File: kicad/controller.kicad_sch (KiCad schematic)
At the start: 26 parts, among them U1 RP2040, U2 W25Q16JVUXIQ, Y1 Crystal_GND24

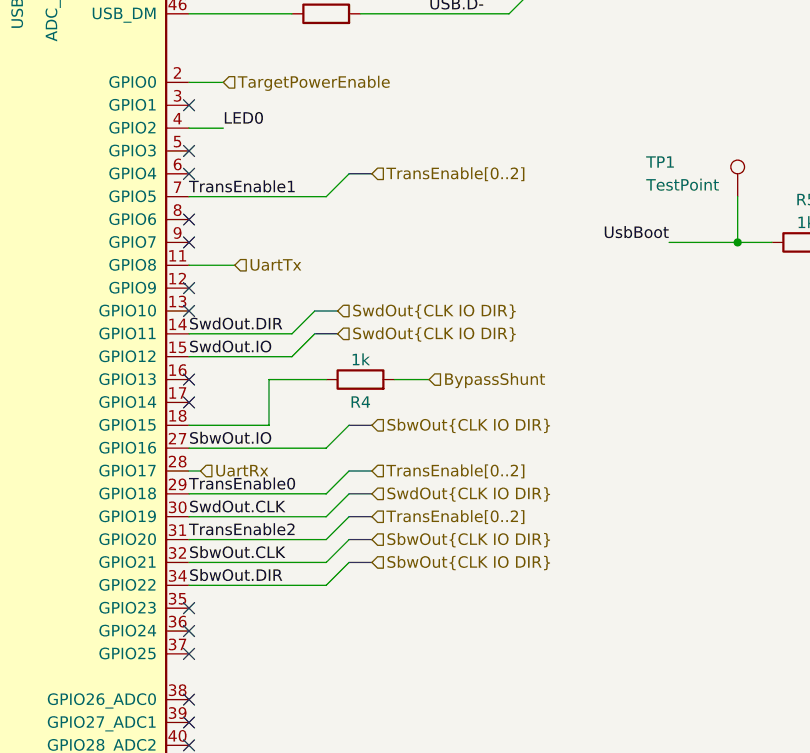
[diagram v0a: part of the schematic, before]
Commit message: add fourth level converter for simultaneous programming + TX/RX
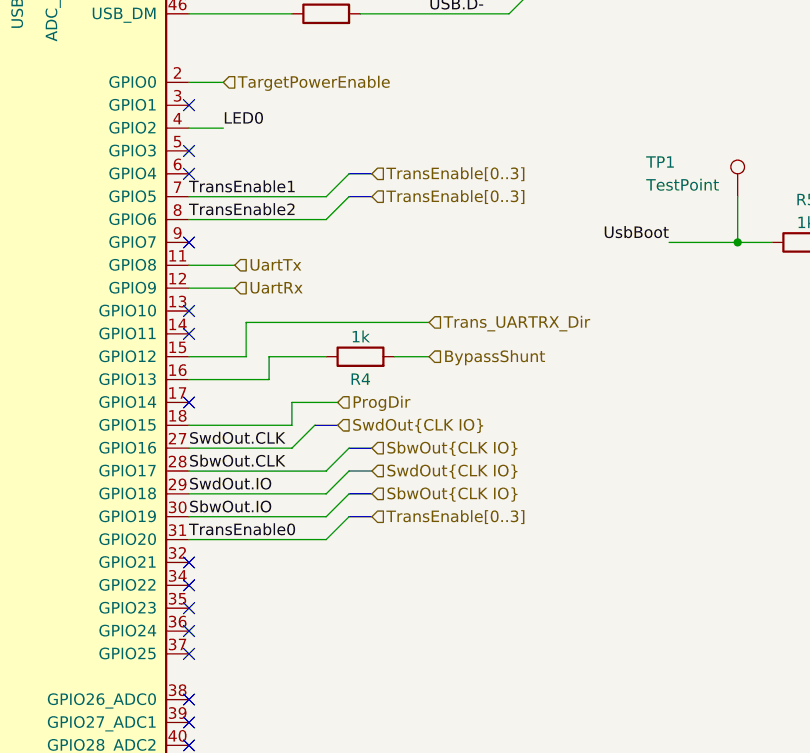
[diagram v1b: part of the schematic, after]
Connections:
- net SbwOut.CLK: now also U1.28 (GPIO17); no longer U1.32 (GPIO21)
- net SbwOut.IO: now also U1.30 (GPIO19); no longer U1.27 (GPIO16)
- net SwdOut.CLK: now also U1.27 (GPIO16); no longer U1.30 (GPIO19)
- net SwdOut.IO: now also U1.29 (GPIO18); no longer U1.15 (GPIO12)
- net TransEnable0: now also U1.31 (GPIO20); no longer U1.29 (GPIO18)
- net TransEnable2: now also U1.8 (GPIO6); no longer U1.31 (GPIO20)
- net UartRx: now also U1.12 (GPIO9); no longer U1.28 (GPIO17)
- net at R4.1: now also U1.16 (GPIO13); no longer U1.18 (GPIO15)
- net SbwOut.DIR: no longer names the net of U1.34 (GPIO22)
- net SwdOut.DIR: no longer names the net of U1.14 (GPIO11)
- new net ProgDir: U1.18 (GPIO15)
- new net Trans_UARTRX_Dir: U1.15 (GPIO12)
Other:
- moved on the sheet: R4

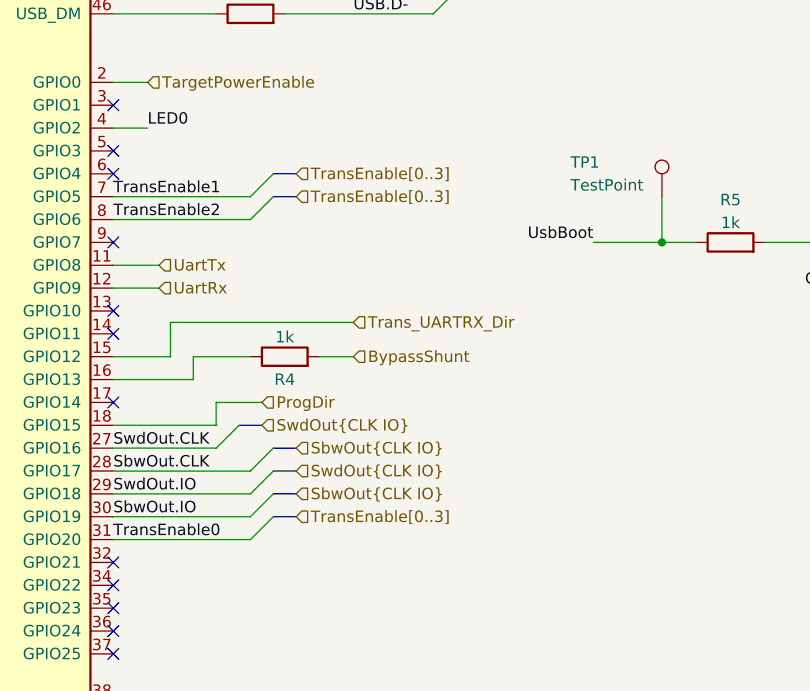
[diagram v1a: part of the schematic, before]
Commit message: fix some net names
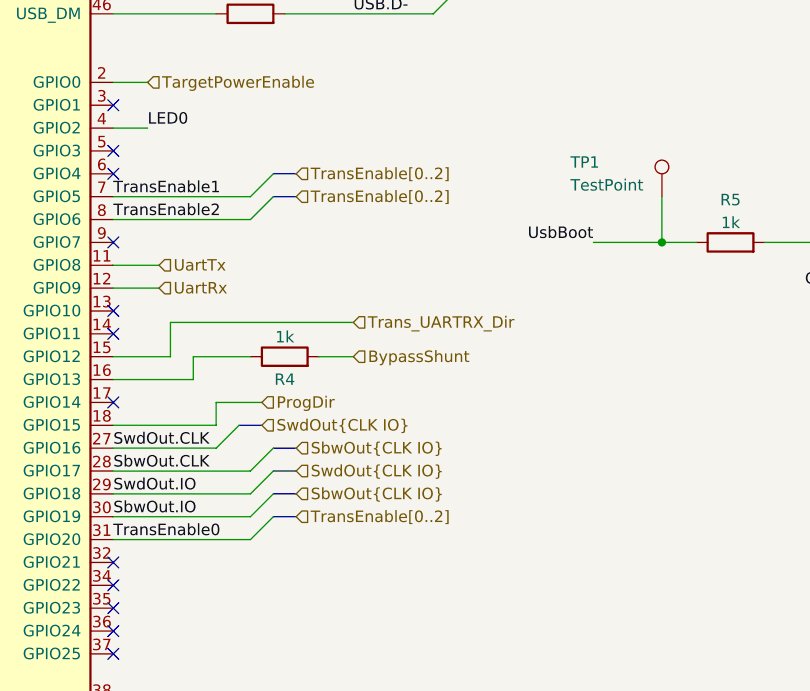
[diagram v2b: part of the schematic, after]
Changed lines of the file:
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@@
     (effects (font (size 1.27 1.27)) (justify left bottom))
   )
-  (hierarchical_label "TransEnable[0..3]" (shape input) (at 171.45 143.51 0)
+  (hierarchical_label "TransEnable[0..2]" (shape input) (at 171.45 143.51 0)
     (effects (font (size 1.27 1.27)) (justify left))
   )
@@
     (effects (font (size 1.27 1.27)) (justify left))
   )
-  (hierarchical_label "TransEnable[0..3]" (shape input) (at 171.45 105.41 0)
+  (hierarchical_label "TransEnable[0..2]" (shape input) (at 171.45 105.41 0)
     (effects (font (size 1.27 1.27)) (justify left))
   )
@@
     (effects (font (size 1.27 1.27)) (justify left))
   )
-  (hierarchical_label "TransEnable[0..3]" (shape input) (at 171.45 107.95 0)
+  (hierarchical_label "TransEnable[0..2]" (shape input) (at 171.45 107.95 0)
     (effects (font (size 1.27 1.27)) (justify left))
   )

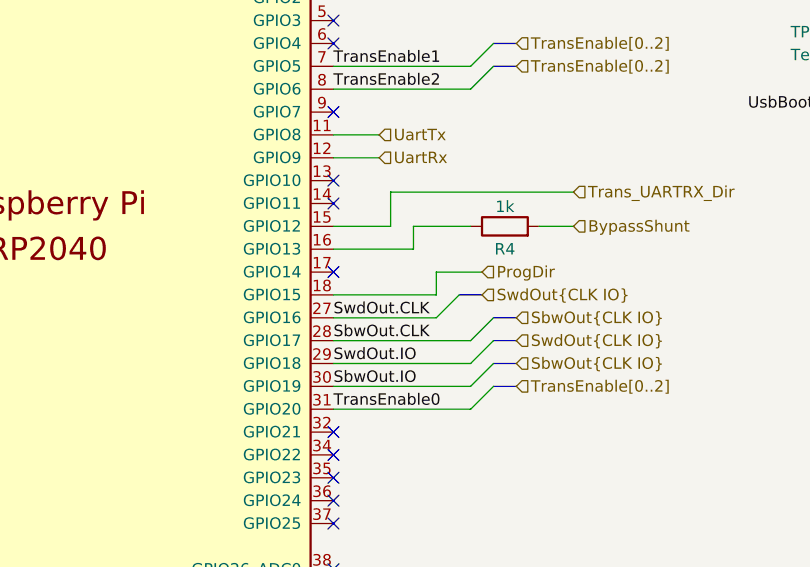
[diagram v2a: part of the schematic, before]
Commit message: replace target supply diode with analog switch
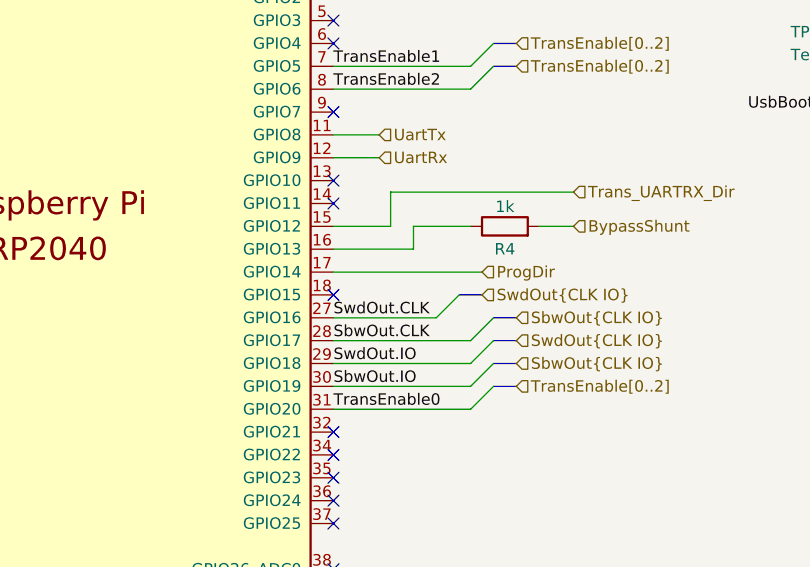
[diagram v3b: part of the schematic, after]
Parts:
- C1, C2: MPN (none) -> 04025A120JAT2A
- C10, C11, C12, C13, C14, C3, C4, C6, C8, C9: MPN (none) -> CL05A104KA5NNNC
- C5, C7: MPN (none) -> CL05A475MP5NRNC
- D1: MPN (none) -> QBLP595-AG1
- R1, R4, R5: MPN (none) -> WR04X1001FTL
- R2, R3: MPN (none) -> CR0402-FX-27R0GLF
- R7: MPN (none) -> CR0402-FX-1200GLF
- U1: MPN (none) -> RP2040
- U2: MPN (none) -> W25Q16JVUXIQ
- Y1: MPN (none) -> RH100-12.000-18-2030-TR
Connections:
- net ProgDir: now also U1.17 (GPIO14); no longer U1.18 (GPIO15)
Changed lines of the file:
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@@
   (no_connect (at 87.63 162.56))
   (no_connect (at 151.13 123.19))
-  (no_connect (at 151.13 130.81))
+  (no_connect (at 151.13 133.35))
   (no_connect (at 151.13 148.59))
   (no_connect (at 151.13 105.41))
@@
     (stroke (width 0) (type default) (color 0 0 0 0))
   )
-  (wire (pts (xy 162.56 130.81) (xy 162.56 133.35))
-    (stroke (width 0) (type default) (color 0 0 0 0))
-  )
   (wire (pts (xy 160.02 128.27) (xy 160.02 125.73))
     (stroke (width 0) (type default) (color 0 0 0 0))
@@
     (stroke (width 0) (type default) (color 0 0 0 0))
   )
-  (wire (pts (xy 162.56 133.35) (xy 151.13 133.35))
-    (stroke (width 0) (type default) (color 0 0 0 0))
-  )
   (wire (pts (xy 151.13 118.11) (xy 156.21 118.11))
     (stroke (width 0) (type default) (color 0 0 0 0))
@@
     (stroke (width 0) (type default) (color 0 0 0 0))
   )
-  (wire (pts (xy 167.64 130.81) (xy 162.56 130.81))
+  (wire (pts (xy 151.13 130.81) (xy 167.64 130.81))
     (stroke (width 0) (type default) (color 0 0 0 0))
   )
@@
     )
     (property "Datasheet" "~" (id 3) (at 142.24 53.34 0)
+      (effects (font (size 1.27 1.27)) hide)
+    )
+    (property "MPN" "CL05A104KA5NNNC" (id 4) (at 142.24 53.34 0)
       (effects (font (size 1.27 1.27)) hide)
     )
@@
       (effects (font (size 1.27 1.27)) hide)
     )
+    (property "MPN" "CR0402-FX-27R0GLF" (id 4) (at 166.37 87.63 0)
+      (effects (font (size 1.27 1.27)) hide)
+    )
     (pin "1")
     (pin "2")
@@
     )
     (property "Datasheet" "~" (id 3) (at 246.38 52.07 0)
+      (effects (font (size 1.27 1.27)) hide)
+    )
+    (property "MPN" "QBLP595-AG1" (id 4) (at 246.38 52.07 0)
       (effects (font (size 1.27 1.27)) hide)
     )
@@
     )
     (property "Datasheet" "~" (id 3) (at 48.26 129.54 0)
+      (effects (font (size 1.27 1.27)) hide)
+    )
+    (property "MPN" "RH100-12.000-18-2030-TR" (id 4) (at 48.26 129.54 0)
       (effects (font (size 1.27 1.27)) hide)
     )
@@
       (effects (font (size 1.27 1.27)) hide)
     )
+    (property "MPN" "WR04X1001FTL" (id 4) (at 170.18 125.73 0)
+      (effects (font (size 1.27 1.27)) hide)
+    )
     (pin "1")
     (pin "2")
@@
     )
     (property "Datasheet" "" (id 3) (at 100.33 128.27 0)
+      (effects (font (size 1.27 1.27)) hide)
+    )
+    (property "MPN" "RP2040" (id 4) (at 119.38 128.27 0)
       (effects (font (size 1.27 1.27)) hide)
     )
@@
       (effects (font (size 1.27 1.27)) hide)
     )
+    (property "MPN" "CL05A104KA5NNNC" (id 4) (at 81.28 53.34 0)
+      (effects (font (size 1.27 1.27)) hide)
+    )
     (pin "1")
     (pin "2")
@@
     )
     (property "Datasheet" "~" (id 3) (at 91.44 53.34 0)
+      (effects (font (size 1.27 1.27)) hide)
+    )
+    (property "MPN" "CL05A104KA5NNNC" (id 4) (at 91.44 53.34 0)
       (effects (font (size 1.27 1.27)) hide)
     )
@@
       (effects (font (size 1.27 1.27)) hide)
     )
+    (property "MPN" "CL05A104KA5NNNC" (id 4) (at 193.04 53.34 0)
+      (effects (font (size 1.27 1.27)) hide)
+    )
     (pin "1")
     (pin "2")
@@
       (effects (font (size 1.27 1.27)) hide)
     )
+    (property "MPN" "04025A120JAT2A" (id 4) (at 31.75 123.19 0)
+      (effects (font (size 1.27 1.27)) hide)
+    )
     (pin "1")
     (pin "2")
@@
     )
     (property "Datasheet" "~" (id 3) (at 91.44 67.31 0)
+      (effects (font (size 1.27 1.27)) hide)
+    )
+    (property "MPN" "CL05A475MP5NRNC" (id 4) (at 91.44 67.31 0)
       (effects (font (size 1.27 1.27)) hide)
     )
@@
     )
     (property "Datasheet" "https://www.winbond.com/resource-files/w25q16jv%20spi%20revh%2004082019%20plus.pdf" (id 3) (at 256.54 138.43 0)
+      (effects (font (size 1.27 1.27)) hide)
+    )
+    (property "MPN" "W25Q16JVUXIQ" (id 4) (at 255.27 115.57 0)
       (effects (font (size 1.27 1.27)) hide)
     )
@@
       (effects (font (size 1.27 1.27)) hide)
     )
+    (property "MPN" "CL05A104KA5NNNC" (id 4) (at 172.72 53.34 0)
+      (effects (font (size 1.27 1.27)) hide)
+    )
     (pin "1")
     (pin "2")
@@
     )
     (property "Datasheet" "~" (id 3) (at 162.56 53.34 0)
+      (effects (font (size 1.27 1.27)) hide)
+    )
+    (property "MPN" "CL05A104KA5NNNC" (id 4) (at 162.56 53.34 0)
       (effects (font (size 1.27 1.27)) hide)
     )
@@
       (effects (font (size 1.27 1.27)) hide)
     )
+    (property "MPN" "WR04X1001FTL" (id 4) (at 219.71 113.03 0)
+      (effects (font (size 1.27 1.27)) hide)
+    )
     (pin "1")
     (pin "2")
@@
       (effects (font (size 1.27 1.27)) hide)
     )
+    (property "MPN" "04025A120JAT2A" (id 4) (at 31.75 135.89 0)
+      (effects (font (size 1.27 1.27)) hide)
+    )
     (pin "1")
     (pin "2")
@@
       (effects (font (size 1.27 1.27)) hide)
     )
+    (property "MPN" "CL05A104KA5NNNC" (id 4) (at 182.88 53.34 0)
+      (effects (font (size 1.27 1.27)) hide)
+    )
     (pin "1")
     (pin "2")
@@
       (effects (font (size 1.27 1.27)) hide)
     )
+    (property "MPN" "CL05A104KA5NNNC" (id 4) (at 261.62 95.25 0)
+      (effects (font (size 1.27 1.27)) hide)
+    )
     (pin "1")
     (pin "2")
@@
     )
     (property "Datasheet" "~" (id 3) (at 142.24 67.31 0)
+      (effects (font (size 1.27 1.27)) hide)
+    )
+    (property "MPN" "CL05A475MP5NRNC" (id 4) (at 142.24 67.31 0)
       (effects (font (size 1.27 1.27)) hide)
     )
@@
       (effects (font (size 1.27 1.27)) hide)
     )
+    (property "MPN" "WR04X1001FTL" (id 4) (at 68.58 135.89 0)
+      (effects (font (size 1.27 1.27)) hide)
+    )
     (pin "1")
     (pin "2")
@@
     )
     (property "Datasheet" "~" (id 3) (at 246.38 43.18 0)
+      (effects (font (size 1.27 1.27)) hide)
+    )
+    (property "MPN" "CR0402-FX-1200GLF" (id 4) (at 246.38 43.18 0)
       (effects (font (size 1.27 1.27)) hide)
     )
@@
       (effects (font (size 1.27 1.27)) hide)
     )
+    (property "MPN" "CR0402-FX-27R0GLF" (id 4) (at 166.37 78.74 0)
+      (effects (font (size 1.27 1.27)) hide)
+    )
     (pin "1")
     (pin "2")
@@
       (effects (font (size 1.27 1.27)) hide)
     )
+    (property "MPN" "CL05A104KA5NNNC" (id 4) (at 152.4 53.34 0)
+      (effects (font (size 1.27 1.27)) hide)
+    )
     (pin "1")
     (pin "2")
@@
       (effects (font (size 1.27 1.27)) hide)
     )
+    (property "MPN" "CL05A104KA5NNNC" (id 4) (at 203.2 53.34 0)
+      (effects (font (size 1.27 1.27)) hide)
+    )

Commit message: refine BOM
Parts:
- R6: now in the parts list
- U1: MPN RP2040 -> SC0914(13)
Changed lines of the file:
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@@
       (effects (font (size 1.27 1.27)) hide)
     )
-    (property "Description" "Cap, 0402, X5R, 10V" (id 5) (at 142.24 53.34 0)
+    (property "Description" "CAP CER 0.1UF 25V X5R 0402" (id 5) (at 142.24 53.34 0)
       (effects (font (size 1.27 1.27)) hide)
     )
@@
       (effects (font (size 1.27 1.27)) hide)
     )
-    (property "Description" "Res, 0402, 1%" (id 5) (at 166.37 87.63 0)
+    (property "Description" "RES SMD 27 OHM 1% 1/16W 0402" (id 5) (at 166.37 87.63 0)
       (effects (font (size 1.27 1.27)) hide)
     )
@@
       (effects (font (size 1.27 1.27)) hide)
     )
-    (property "Description" "LED, 0402, green, clear" (id 5) (at 246.38 52.07 0)
+    (property "Description" "LED GREEN CLEAR 0402 SMD" (id 5) (at 246.38 52.07 0)
       (effects (font (size 1.27 1.27)) hide)
     )
@@
       (effects (font (size 1.27 1.27)) hide)
     )
-    (property "Description" "12MHZ 18PF Crystal" (id 5) (at 48.26 129.54 0)
+    (property "Description" "CRYSTAL 12.0MHZ 18PF SMD" (id 5) (at 48.26 129.54 0)
       (effects (font (size 1.27 1.27)) hide)
     )
@@
       (effects (font (size 1.27 1.27)) hide)
     )
-    (property "Description" "Res, 0402, 1%" (id 5) (at 170.18 125.73 0)
+    (property "Description" "RES 1K OHM 1% 1/16W 0402" (id 5) (at 170.18 125.73 0)
       (effects (font (size 1.27 1.27)) hide)
     )
@@
       (effects (font (size 1.27 1.27)) hide)
     )
-    (property "MPN" "RP2040" (id 4) (at 119.38 128.27 0)
+    (property "MPN" "SC0914(13)" (id 4) (at 119.38 128.27 0)
+      (effects (font (size 1.27 1.27)) hide)
+    )
+    (property "Description" "IC MCU 32BIT EXT MEM 56QFN" (id 5) (at 119.38 128.27 0)
       (effects (font (size 1.27 1.27)) hide)
     )
@@
       (effects (font (size 1.27 1.27)) hide)
     )
-    (property "Description" "Cap, 0402, X5R, 10V" (id 5) (at 81.28 53.34 0)
+    (property "Description" "CAP CER 0.1UF 25V X5R 0402" (id 5) (at 81.28 53.34 0)
       (effects (font (size 1.27 1.27)) hide)
     )
@@
       (effects (font (size 1.27 1.27)) hide)
     )
-    (property "Description" "Cap, 0402, X5R, 10V" (id 5) (at 91.44 53.34 0)
+    (property "Description" "CAP CER 0.1UF 25V X5R 0402" (id 5) (at 91.44 53.34 0)
       (effects (font (size 1.27 1.27)) hide)
     )
@@
   )
   (symbol (lib_id "Device:R") (at 240.03 101.6 0) (unit 1)
-    (in_bom no) (on_board yes) (fields_autoplaced)
+    (in_bom yes) (on_board yes) (fields_autoplaced)
     (property "Reference" "R6" (id 0) (at 241.808 100.7653 0)
       (effects (font (size 1.27 1.27)) (justify left))
@@
     )
     (property "Datasheet" "~" (id 3) (at 240.03 101.6 0)
+      (effects (font (size 1.27 1.27)) hide)
+    )
+    (property "Description" "DO NOT PLACE" (id 4) (at 240.03 101.6 0)
       (effects (font (size 1.27 1.27)) hide)
     )
@@
       (effects (font (size 1.27 1.27)) hide)
     )
-    (property "Description" "Cap, 0402, X5R, 10V" (id 5) (at 193.04 53.34 0)
+    (property "Description" "CAP CER 0.1UF 25V X5R 0402" (id 5) (at 193.04 53.34 0)
       (effects (font (size 1.27 1.27)) hide)
     )
@@
       (effects (font (size 1.27 1.27)) hide)
     )
-    (property "Description" "Cap, 0402, C0G/NP0, 50V, 5%" (id 5) (at 31.75 123.19 0)
+    (property "Description" "CAP CER 12PF 50V C0G/NP0 0402" (id 5) (at 31.75 123.19 0)
       (effects (font (size 1.27 1.27)) hide)
     )
@@
       (effects (font (size 1.27 1.27)) hide)
     )
-    (property "Description" "Cap, 0402, X5R, 10V" (id 5) (at 91.44 67.31 0)
+    (property "Description" "CAP CER 4.7UF 10V X5R 0402" (id 5) (at 91.44 67.31 0)
       (effects (font (size 1.27 1.27)) hide)
     )
@@
       (effects (font (size 1.27 1.27)) hide)
     )
-    (property "Description" "Cap, 0402, X5R, 10V" (id 5) (at 172.72 53.34 0)
+    (property "Description" "CAP CER 0.1UF 25V X5R 0402" (id 5) (at 172.72 53.34 0)
       (effects (font (size 1.27 1.27)) hide)
     )
@@
       (effects (font (size 1.27 1.27)) hide)
     )
-    (property "Description" "Cap, 0402, X5R, 10V" (id 5) (at 162.56 53.34 0)
+    (property "Description" "CAP CER 0.1UF 25V X5R 0402" (id 5) (at 162.56 53.34 0)
       (effects (font (size 1.27 1.27)) hide)
     )
@@
       (effects (font (size 1.27 1.27)) hide)
     )
-    (property "Description" "Res, 0402, 1%" (id 5) (at 219.71 113.03 0)
+    (property "Description" "RES 1K OHM 1% 1/16W 0402" (id 5) (at 219.71 113.03 0)
       (effects (font (size 1.27 1.27)) hide)
     )
@@
       (effects (font (size 1.27 1.27)) hide)
     )
-    (property "Description" "Cap, 0402, C0G/NP0, 50V, 5%" (id 5) (at 31.75 135.89 0)
+    (property "Description" "CAP CER 12PF 50V C0G/NP0 0402" (id 5) (at 31.75 135.89 0)
       (effects (font (size 1.27 1.27)) hide)
     )
@@
       (effects (font (size 1.27 1.27)) hide)
     )
-    (property "Description" "Cap, 0402, X5R, 10V" (id 5) (at 182.88 53.34 0)
+    (property "Description" "CAP CER 0.1UF 25V X5R 0402" (id 5) (at 182.88 53.34 0)
       (effects (font (size 1.27 1.27)) hide)
     )
@@
       (effects (font (size 1.27 1.27)) hide)
     )
-    (property "Description" "Cap, 0402, X5R, 10V" (id 5) (at 261.62 95.25 0)
+    (property "Description" "CAP CER 0.1UF 25V X5R 0402" (id 5) (at 261.62 95.25 0)
       (effects (font (size 1.27 1.27)) hide)
     )
@@
       (effects (font (size 1.27 1.27)) hide)
     )
-    (property "Description" "Cap, 0402, X5R, 10V" (id 5) (at 142.24 67.31 0)
+    (property "Description" "CAP CER 4.7UF 10V X5R 0402" (id 5) (at 142.24 67.31 0)
       (effects (font (size 1.27 1.27)) hide)
     )
@@
       (effects (font (size 1.27 1.27)) hide)
     )
-    (property "Description" "Res, 0402, 1%" (id 5) (at 68.58 135.89 0)
+    (property "Description" "RES 1K OHM 1% 1/16W 0402" (id 5) (at 68.58 135.89 0)
       (effects (font (size 1.27 1.27)) hide)
     )
@@
       (effects (font (size 1.27 1.27)) hide)
     )
-    (property "Description" "Res, 0402, 1%" (id 5) (at 246.38 43.18 0)
+    (property "Description" "RES SMD 120 OHM 1% 1/16W 0402" (id 5) (at 246.38 43.18 0)
       (effects (font (size 1.27 1.27)) hide)
     )
@@
       (effects (font (size 1.27 1.27)) hide)
     )
-    (property "Description" "Res, 0402, 1%" (id 5) (at 166.37 78.74 0)
+    (property "Description" "RES SMD 27 OHM 1% 1/16W 0402" (id 5) (at 166.37 78.74 0)
       (effects (font (size 1.27 1.27)) hide)
     )
@@
       (effects (font (size 1.27 1.27)) hide)
     )
-    (property "Description" "Cap, 0402, X5R, 10V" (id 5) (at 152.4 53.34 0)
+    (property "Description" "CAP CER 0.1UF 25V X5R 0402" (id 5) (at 152.4 53.34 0)
       (effects (font (size 1.27 1.27)) hide)
     )
@@
       (effects (font (size 1.27 1.27)) hide)
     )
-    (property "Description" "Cap, 0402, X5R, 10V" (id 5) (at 203.2 53.34 0)
-      (effects (font (size 1.27 1.27)) hide)
-    )
+    (property "Description" "CAP CER 0.1UF 25V X5R 0402" (id 5) (at 203.2 53.34 0)
+      (effects (font (size 1.27 1.27)) hide)
+    )
